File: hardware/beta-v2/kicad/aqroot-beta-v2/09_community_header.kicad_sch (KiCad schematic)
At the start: 36 parts, among them J5 COMMUNITY_HEADER_2x13, U15 TPS22918, U16 TCA9517ADGK

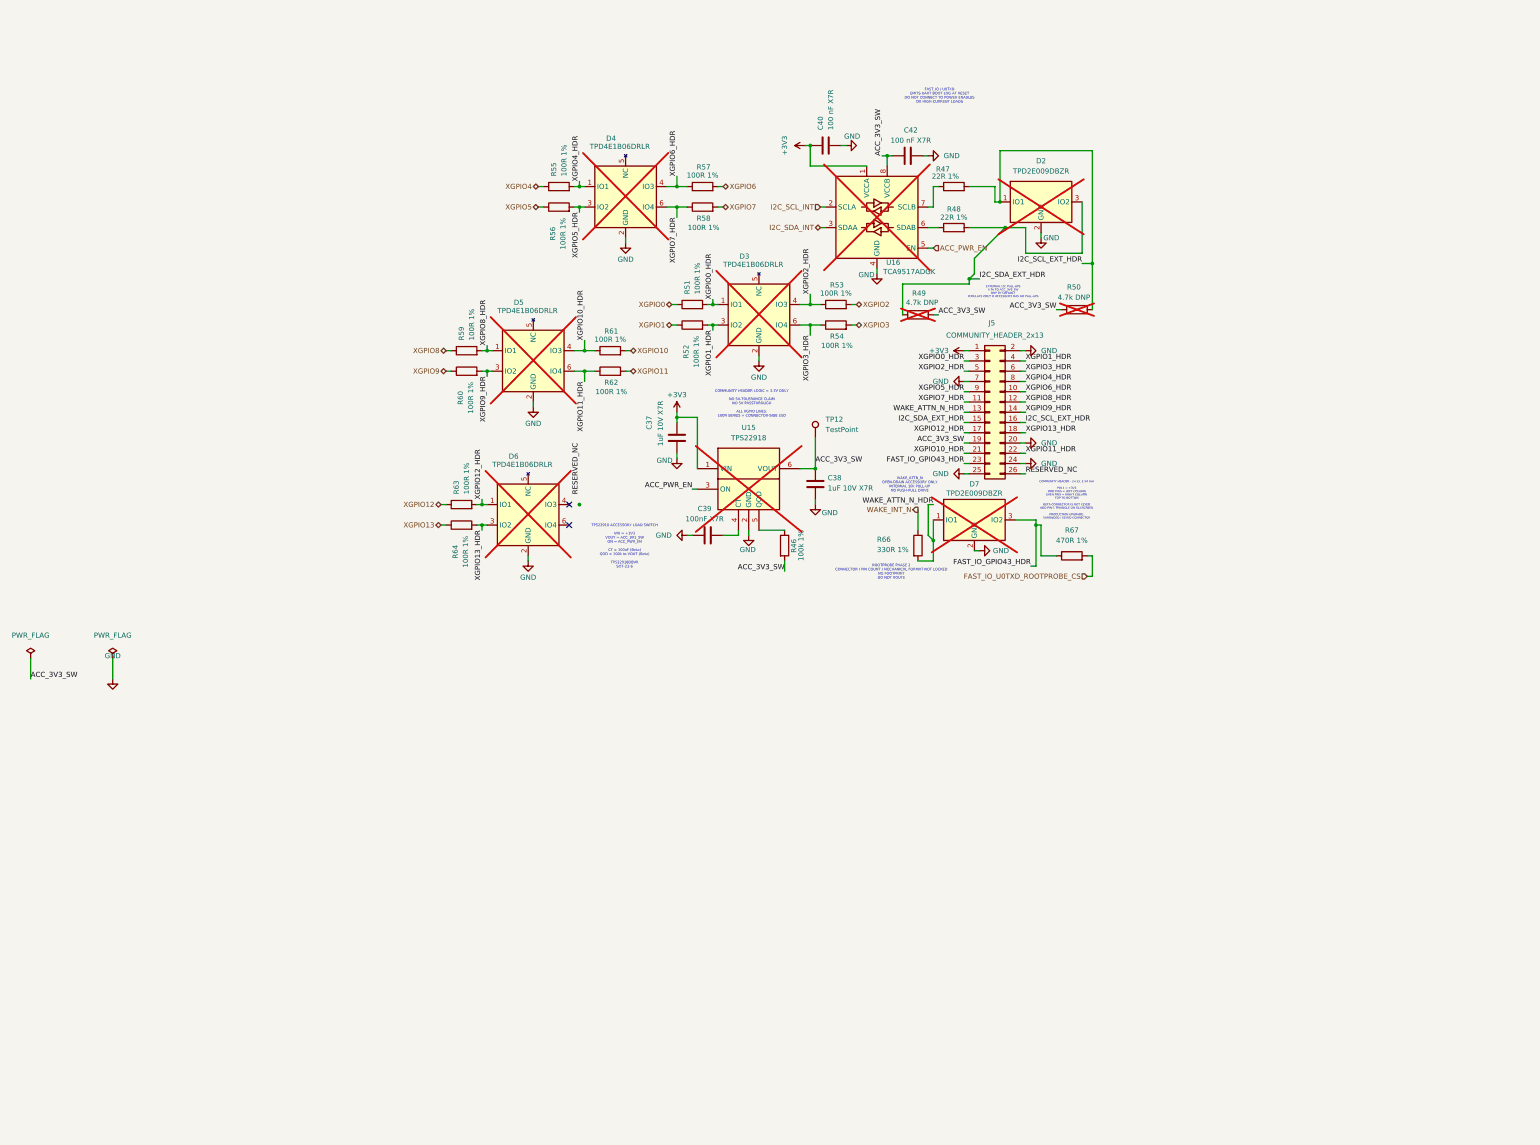
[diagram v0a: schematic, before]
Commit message: hardware: migrate Full Beta v2 community expansion
Sheet 09 migrated (FBV2-S1-009). All nine schematic sheets now carry the Full
Beta v2 architecture and fork_equivalence.py's "still Beta-DM" list is empty.

Three CTO rulings implemented. O-6 ratified: U23, the third PCAL9535APW,118 at
0x22, and the front RGB are locked architecture; B-37 retired with 11 spare
expander pins. O-4 approved: U16 TCA9517A -> TI TCA4307DGKR (LCSC C880333),
FITTED where the old part was DNP. P-18 closed with no I2C mux.

Sheet 09 was rebuilt, not patched, and was hiding two serious defects: J5
contact 1 carried permanent raw +3V3 against D-057, and the community port had
no power at all - 01:ACC_3V3_SW and 09:ACC_3V3_SW were different nets, the
latter fed by a second, DNP TPS22918. Also removed: the 26-pin 2x13 male
header, XGPIO10-13, FAST_IO_GPIO43_HDR, RESERVED_NC. Sixth consecutive sheet
with a load-bearing inherited DNP.

Connector footprint built from the Samtec RECOMMENDED PCB LAYOUT REV B FIG 3:
2.54 mm in row, 7.87 +/-0.05 mm row-to-row, 0.71 mm PTH, 27.94 mm pin field.
All 24 contacts verified pin by pin against D-084.

External I2C pull-ups re-derived: the inherited 4.7k gives 796 ns against a
300 ns fast-mode budget at 200 pF and could never have worked; now 1.5k =
254 ns. Both current limits re-derived rather than copied - 3.3 V stays 1.5k
but the accessory-short case moved 86% -> 89% of the TPS63020's 2 A.

5 V enables split per the CTO refinement: ACC_5V_BOOST_EN on U3 P13 and
ACC_5V_SW_EN on U23 P04, each with its own 100k pull-down. B-08 closed in
copper with Q10, source facing the connector. All six TVS arrays were DNP and
are now fitted; one TPD4E1B06DRLR MPN covers all sixteen exposed contacts.

#FLG0105, deleted by the rebuild, turned out to be the only power-output driver
on the entire GND net and was re-created with a note explaining its role.

ERC 42/1/41 -> 27/0/27 - zero errors for the first time. 321 components, 0
duplicate references, 0 without a footprint, 224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
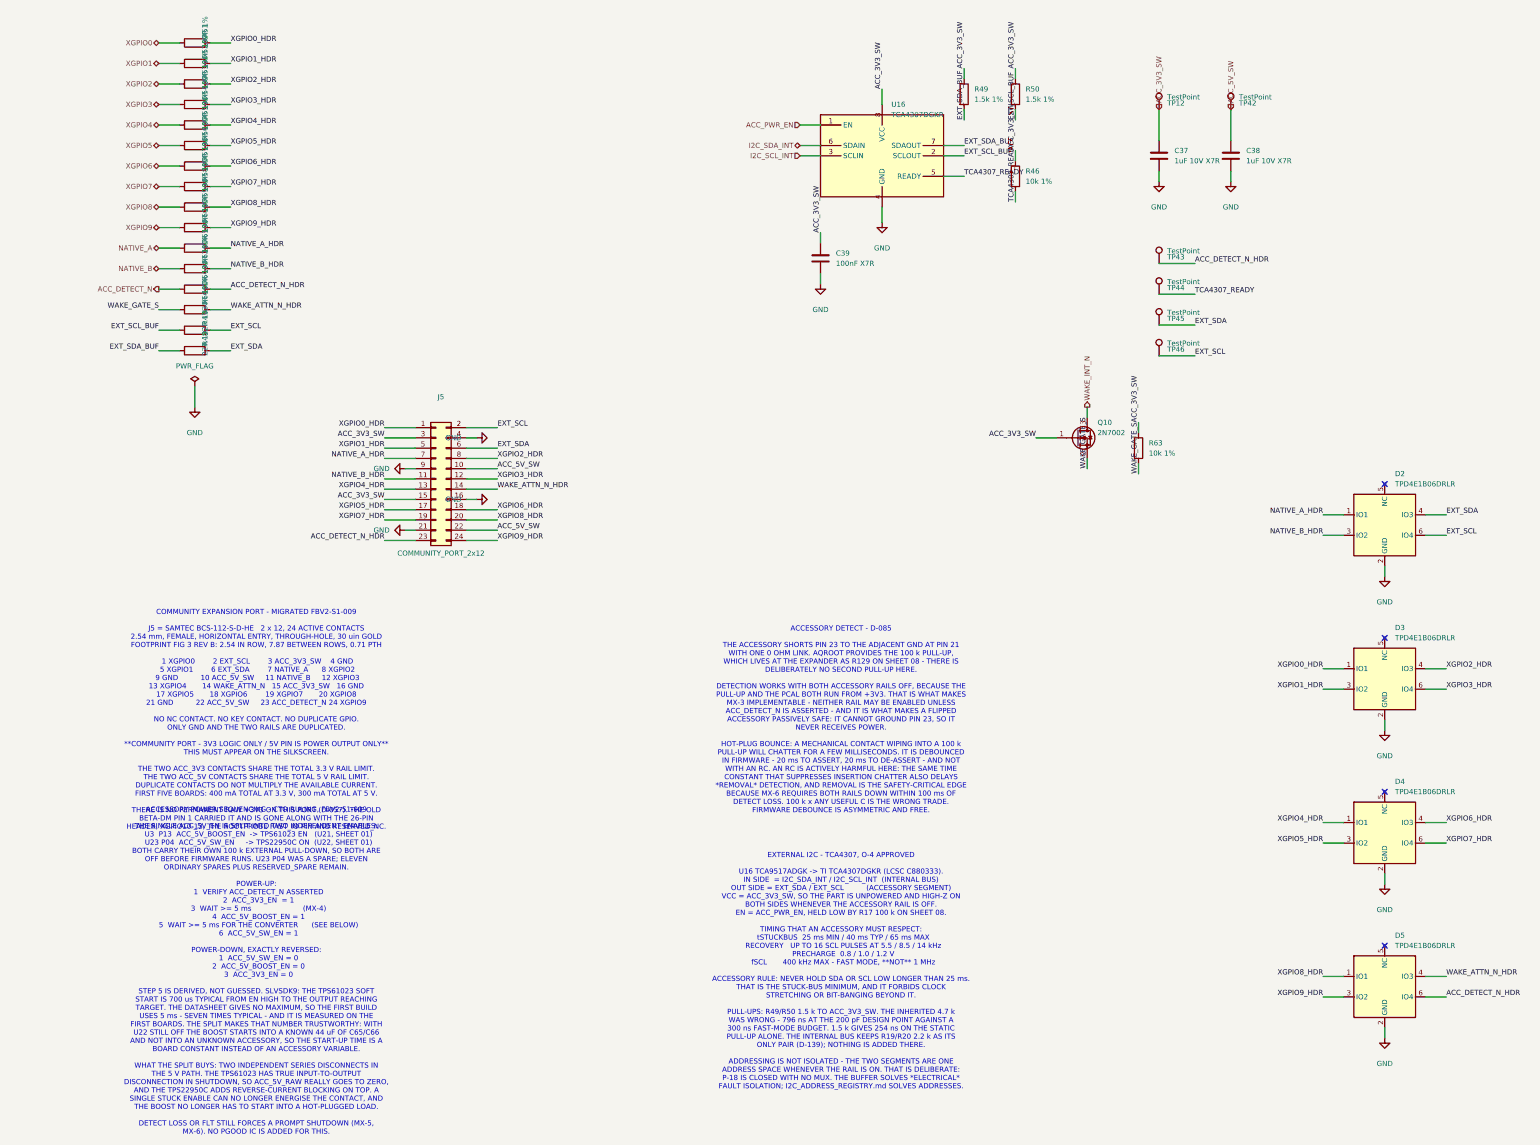
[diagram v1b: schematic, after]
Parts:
- removed C40, C42: 100 nF X7R, Capacitor_SMD:C_0603_1608Metric, symbol Device:C
- removed D2, D7: TPD2E009DBZR, Package_TO_SOT_SMD:SOT-23, symbol AQROOT_Beta:TPD2E009DBZR
- removed D6: TPD4E1B06DRLR, Package_TO_SOT_SMD:SOT-563, symbol AQROOT_Beta:TPD4E1B06DRLR
- removed J5: COMMUNITY_HEADER_2x13, AQROOT_Beta:Samtec_TSW-113-08-G-D-RA, symbol Connector_Generic:Conn_02x13_Odd_Even
- removed R67: 470R 1%, Resistor_SMD:R_0603_1608Metric, symbol Device:R
- removed U15: TPS22918, Package_TO_SOT_SMD:SOT-23-6, symbol AQROOT_Beta:TPS22918
- removed U16: TCA9517ADGK, Package_SO:VSSOP-8_3x3mm_P0.65mm, symbol Logic_LevelTranslator:TCA9517ADGK
- added D2: TPD4E1B06DRLR, Package_TO_SOT_SMD:SOT-563, symbol AQROOT_Beta:TPD4E1B06DRLR
- added J5: COMMUNITY_PORT_2x12, AQROOT_Beta:Samtec_BCS-112-S-D-HE, symbol Connector_Generic:Conn_02x12_Odd_Even
- added Q10: 2N7002, Package_TO_SOT_SMD:SOT-23, symbol Transistor_FET:Q_NMOS_GSD
- added TP42, TP43, TP44, TP45, TP46: TestPoint, TestPoint:TestPoint_Pad_D1.0mm, symbol Connector:TestPoint
- added U16: TCA4307DGKR, Package_SO:VSSOP-8_3x3mm_P0.65mm, symbol AQROOT_Beta:TCA4307DGKR
- C37: Note (none) -> Accessory 3.3 V rail decoupling AT THE CONNECTOR, FBV2-S1-0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
- C38: Note (none) -> Accessory 5 V rail decoupling AT THE CONNECTOR, FBV2-S1-009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
- C39: Note (none) -> TCA4307 local decoupling, FBV2-S1-009. 100 nF X7R 0603 agai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
- D3, D4, D5: Note Four independent bidirectional ESD channels. Place on the c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 -> Low-capacitance ESD array on the exposed community contacts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; Package SOT-563, TI DRL -> (none); now fitted
- R46: value 100k 1% -> 10k 1%; Note (none) -> TCA4307 READY pull-up, FBV2-S1-009. READY is an OPEN-DRAIN 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; Power (none) -> 0.1W; Tolerance (none) -> 1%
- R47, R48: Note (none) -> External I2C series element, D-090, RE-DERIVED FOR THE TCA4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; Power (none) -> 0.1W; Tolerance (none) -> 1%
- R49: value 4.7k DNP -> 1.5k 1%; Note (none) -> EXTERNAL I2C SDA pull-up, RE-DERIVED FBV2-S1-009. THE INHER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; Power (none) -> 0.1W; Tolerance (none) -> 1%; now fitted
- R50: value 4.7k DNP -> 1.5k 1%; Note (none) -> EXTERNAL I2C SCL pull-up, RE-DERIVED FBV2-S1-009. THE INHER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; Power (none) -> 0.1W; Tolerance (none) -> 1%; now fitted
- R51, R52, R53, R54, R55, R56, R57, R58, R59, R60: Note (none) -> Community XGPIO series protection, D-090. 100 Ohm between t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; Power (none) -> 0.1W; Tolerance (none) -> 1%
- R61, R62: Note (none) -> Native community pin series protection, D-090. 100 Ohm betw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; Power (none) -> 0.1W; Tolerance (none) -> 1%
- R63: value 100R 1% -> 10k 1%; Note (none) -> WAKE contact pull-up, FBV2-S1-009. 10 kOhm from the accesso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; Power (none) -> 0.1W; Tolerance (none) -> 1%
- R64: Note (none) -> ACC_DETECT_N series protection, ADDED FBV2-S1-009. D-090 di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; Power (none) -> 0.1W; Tolerance (none) -> 1%
- R66: Note (none) -> WAKE series protection, D-090. 330 Ohm rather than 100 Ohm 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; Power (none) -> 0.1W; Tolerance (none) -> 1%
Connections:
- net +3V3 is gone; now on net ACC_3V3_SW: C37.1
- net XGPIO12 is gone; now on net ACC_3V3_SW: R63.1
- net XGPIO13_HDR is gone; now on net ACC_DETECT_N_HDR: R64.2
- net ACC_3V3_SW: now also C39.1, R46.1, R49.1, R50.1, J5.15 (Pin_15), J5.3 (Pin_3), Q10.1 (G), U16.8 (VCC); no longer C38.1, R46.2, R49.2, R50.2
- net ACC_PWR_EN: now also U16.1 (EN)
- net GND: now also C39.2, D2.2 (GND), J5.16 (Pin_16), J5.21 (Pin_21), J5.4 (Pin_4), J5.9 (Pin_9), U16.4 (GND); no longer C39.1
- net I2C_SCL_INT: now also U16.3 (SCLIN)
- net I2C_SDA_INT: now also U16.6 (SDAIN)
- net WAKE_ATTN_N_HDR: now also D5.4 (IO3), J5.14 (Pin_14)
- net WAKE_INT_N: now also Q10.3 (D); no longer R66.1
- net XGPIO0_HDR: now also J5.1 (Pin_1)
- net XGPIO1_HDR: now also J5.5 (Pin_5)
- net XGPIO2: now also R53.1; no longer R53.2
- net XGPIO2_HDR: now also R53.2, J5.8 (Pin_8); no longer R53.1
- net XGPIO3: now also R54.1; no longer R54.2
- net XGPIO3_HDR: now also R54.2, J5.12 (Pin_12); no longer R54.1
- net XGPIO4_HDR: now also J5.13 (Pin_13)
- net XGPIO5_HDR: now also J5.17 (Pin_17)
- net XGPIO6: now also R57.1; no longer R57.2
- net XGPIO6_HDR: now also R57.2, J5.18 (Pin_18); no longer R57.1
- net XGPIO7: now also R58.1; no longer R58.2
- net XGPIO7_HDR: now also R58.2, J5.19 (Pin_19); no longer R58.1
- net XGPIO8_HDR: now also J5.20 (Pin_20)
- net XGPIO9_HDR: now also J5.24 (Pin_24)
- net EXT_SCL_BUF: now reaches R47.1
- net EXT_SCL_BUF: now also R50.2, U16.2 (SCLOUT)
- net EXT_SDA_BUF: now reaches R48.1
- net EXT_SDA_BUF: now also R49.2, U16.7 (SDAOUT)
- net I2C_SCL_EXT_HDR renamed EXT_SCL
- net EXT_SCL: now also D2.6 (IO4), J5.2 (Pin_2), TP46.1; no longer R50.1
- net I2C_SDA_EXT_HDR renamed EXT_SDA
- net EXT_SDA: now also D2.4 (IO3), J5.6 (Pin_6), TP45.1; no longer R49.1
- net XGPIO10 renamed NATIVE_A_HDR
- net NATIVE_A_HDR: now also D2.1 (IO1), J5.7 (Pin_7)
- net XGPIO10_HDR renamed NATIVE_A
- net NATIVE_A: no longer D5.4 (IO3)
- net XGPIO11 renamed NATIVE_B_HDR
- net NATIVE_B_HDR: now also D2.3 (IO2), J5.11 (Pin_11)
- net XGPIO11_HDR renamed ACC_DETECT_N_HDR
- net ACC_DETECT_N_HDR: now also J5.23 (Pin_23), TP43.1; no longer R62.1
- net XGPIO12_HDR renamed WAKE_GATE_S
- net WAKE_GATE_S: now also R66.1, Q10.2 (S)
- net XGPIO13 renamed ACC_DETECT_N
- new net ACC_5V_SW: C38.1, J5.10 (Pin_10), J5.22 (Pin_22), TP42.1
- new net NATIVE_B: R62.1
- new net TCA4307_READY: R46.2, TP44.1, U16.5 (READY)
- no-connect marks 2 -> 4
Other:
- note added: "ACCESSORY DETECT - D-085 THE ACCESSORY SHORTS PIN 23 TO THE ADJACENT GND AT PIN 21 WITH ONE 0 OHM LINK. AQROOT PROVIDES THE 100 k PULL-UP, WHICH LIVES AT THE EXPANDER AS R129 ON SHEET 08 - THERE IS DELIBERATELY NO SECOND PULL-UP HERE. DETECTION WORKS WITH BOTH ACCESSORY RAILS OFF, BECAUSE THE PULL-UP AND THE PCAL BOTH RUN FROM +3V3. THAT IS WHAT MAKES MX-3 IMPLEMENTABLE - NEITHER RAIL MAY BE ENAB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"
- note added: "ACCESSORY POWER SEQUENCING - CTO RULING, FBV2-S1-009 THE SINGLE ACC_5V_EN IS SPLIT INTO TWO INDEPENDENT ENABLES: U3 P13 ACC_5V_BOOST_EN -> TPS61023 EN (U21, SHEET 01) U23 P04 ACC_5V_SW_EN -> TPS22950C ON (U22, SHEET 01) BOTH CARRY THEIR OWN 100 k EXTERNAL PULL-DOWN, SO BOTH ARE OFF BEFORE FIRMWARE RUNS. U23 P04 WAS A SPARE; ELEVEN ORDINARY SPARES PLUS RESERVED_SPARE REMAIN. POWER-UP: 1 VERIFY ACC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"
- note added: "COMMUNITY EXPANSION PORT - MIGRATED FBV2-S1-009 J5 = SAMTEC BCS-112-S-D-HE 2 x 12, 24 ACTIVE CONTACTS 2.54 mm, FEMALE, HORIZONTAL ENTRY, THROUGH-HOLE, 30 uin GOLD FOOTPRINT FIG 3 REV B: 2.54 IN ROW, 7.87 BETWEEN ROWS, 0.71 PTH 1 XGPIO0 2 EXT_SCL 3 ACC_3V3_SW 4 GND 5 XGPIO1 6 EXT_SDA 7 NATIVE_A 8 XGPIO2 9 GND 10 ACC_5V_SW 11 NATIVE_B 12 XGPIO3 13 XGPIO4 14 WAKE_ATTN_N 15 ACC_3V3_SW 16 GND 17 XGPIO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"
- note added: "EXTERNAL I2C - TCA4307, O-4 APPROVED U16 TCA9517ADGK -> TI TCA4307DGKR (LCSC C880333). IN SIDE = I2C_SDA_INT / I2C_SCL_INT (INTERNAL BUS) OUT SIDE = EXT_SDA / EXT_SCL (ACCESSORY SEGMENT) VCC = ACC_3V3_SW, SO THE PART IS UNPOWERED AND HIGH-Z ON BOTH SIDES WHENEVER THE ACCESSORY RAIL IS OFF. EN = ACC_PWR_EN, HELD LOW BY R17 100 k ON SHEET 08. TIMING THAT AN ACCESSORY MUST RESPECT: tSTUCKBUS 25 ms M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"
- note removed: "COMMUNITY HEADER - 2×13, 2.54 mm PIN 1 = +3V3 ODD PINS = LEFT COLUMN EVEN PINS = RIGHT COLUMN TOP TO BOTTOM BETA CONNECTOR IS NOT KEYED ADD PIN-1 TRIANGLE ON SILKSCREEN PRODUCTION UPGRADE: SHROUDED / KEYED CONNECTOR"
- note removed: "COMMUNITY HEADER LOGIC = 3.3V ONLY NO 5V-TOLERANCE CLAIM NO 5V PASSTHROUGH ALL XGPIO LINES: 100R SERIES + CONNECTOR-SIDE ESD"
- note removed: "EXTERNAL I2C PULL-UPS 4.7k TO ACC_3V3_SW DNP BY DEFAULT POPULATE ONLY IF ACCESSORY HAS NO PULL-UPS"
- note removed: "FAST_IO / U0TXD EMITS UART BOOT LOG AT RESET DO NOT CONNECT TO POWER ENABLES OR HIGH-CURRENT LOADS"
- note removed: "ROOTPROBE PHASE 2 CONNECTOR / PIN COUNT / MECHANICAL FORMAT NOT LOCKED NO FOOTPRINT DO NOT ROUTE"
- note removed: "TPS22918 ACCESSORY LOAD SWITCH VIN = +3V3 VOUT = ACC_3V3_SW ON = ACC_PWR_EN CT = 100nF (Beta) QOD = 100k to VOUT (Beta) TPS22918DBVR SOT-23-6"
- note removed: "WAKE_ATTN_N OPEN-DRAIN ACCESSORY ONLY INTERNAL 10k PULL-UP NO PUSH-PULL DRIVE"

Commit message: hardware: close Full Beta v2 S2 release blockers
Closes B-03, B-63, B-70 and B-71's schematic-side work. Property-only
changes to the nine sheets plus the microphone footprint; ERC unchanged
at 27 / 0 errors / 27 with an identical violation histogram, and the PCB
is untouched and still bit-identical to Beta-DM.

B-03 - all eight remaining Tier-2 footprints compared dimension by
dimension against retrieved manufacturer drawings. Y1 moves from
candidate to lock (Yajingxin TXM27.12M0004322DBBDO00T, C362365, 3421 in
stock) with a land that matches the vendor's Suggested Layout exactly.
The MAX98357A looked like a genuine defect - outline 21-0136 gives
T1633-5 an EP of 1.50/1.60/1.70 while the land is 1.23 - and is not:
land pattern 90-0032 Rev E is issued for T1633-5, -5C and -7C together
and specifies one land for all three, so no project-local footprint was
created.

B-63 - the microphone acoustic port is now drawn rather than described.
1.05 mm NPTH taken from the drawing's own pad-4 ring inner diameter,
paste pulled back 0.10 mm as a declared stencil choice, keepout marked,
bottom-port orientation recorded.

B-70 - L5/L6 lock to Murata LQW18AN39NG80D. The DCR is a first-order
term here: 0.20 ohm max against R_q = 1.1 ohm drops network Q from 25.3
to about 21.4, so the antenna must be tuned with this exact part fitted
and the first lever is R_q, not 39 nH.

B-71 - 65 LCSC fields written in, three MPN strings corrected. J6 and J7
carried bare order codes that resolve to zero-stock listings while the
plating-suffixed strings are abundantly stocked. Six substitution traps
recorded in the symbols themselves, including BAT54W offered for
BAT54WS - a single diode for a series pair - and a clone for the battery
reverse-polarity pass FETs.

Eight DNP parts still carried no recorded reason and now do. The design
has zero unexplained DNP.

Co-Authored-By: Claude Opus 5 <noreply@anthropic.com>
Claude-Session: https://claude.ai/code/session_0133CdFHfKcCH8oPWqJZWe7o
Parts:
- D2, D3, D4, D5: LCSC (none) -> C1972953
- J5: LCSC (none) -> C5575816; Note2 (none) -> SOURCING 2026-08-23 (FBV2-S2-002) (B-71). Samtec BCS-112-S-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
- Q10: LCSC (none) -> C8545
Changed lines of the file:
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@@
 			)
 		)
+		(property "Note2" "SOURCING 2026-08-23 (FBV2-S2-002) (B-71). Samtec BCS-112-S-D-HE is LCSC C5575816 with STOCK 0 at $15.54. It is a 24-contact through-hole strip and was already MANUAL/SECONDARY ASSEMBLY by CTO ruling at FBV2-S1-009; buy direct from Samtec or a broadline distributor. The connector architecture is NOT compromised for SMT assembly. LCSC/JLC library state verified live on 2026-08-23 through the JLCPCB parts API (D-096). Stock is a snapshot, not a guarantee."
+			(at 120.65 140.97 0)
+			(hide yes)
+			(show_name no)
+			(do_not_autoplace no)
+			(effects
+				(font
+					(size 1.27 1.27)
+				)
+			)
+		)
+		(property "LCSC" "C5575816"
+			(at 120.65 140.97 0)
+			(hide yes)
+			(show_name no)
+			(do_not_autoplace no)
+			(effects
+				(font
+					(size 1.27 1.27)
+				)
+			)
+		)
 		(property "Manufacturer" "Samtec"
 			(at 0 0 0)
@@
 			)
 		)
+		(property "LCSC" "C8545"
+			(at 279.4 130.81 0)
+			(hide yes)
+			(show_name no)
+			(do_not_autoplace no)
+			(effects
+				(font
+					(size 1.27 1.27)
+				)
+			)
+		)
 		(property "Manufacturer" "onsemi"
 			(at 0 0 0)
@@
 			)
 		)
+		(property "LCSC" "C1972953"
+			(at 355.6 152.4 0)
+			(hide yes)
+			(show_name no)
+			(do_not_autoplace no)
+			(effects
+				(font
+					(size 1.27 1.27)
+				)
+			)
+		)
 		(property "Manufacturer" "Texas Instruments"
 			(at 0 0 0)
@@
 			)
 		)
+		(property "LCSC" "C1972953"
+			(at 355.6 190.5 0)
+			(hide yes)
+			(show_name no)
+			(do_not_autoplace no)
+			(effects
+				(font
+					(size 1.27 1.27)
+				)
+			)
+		)
 		(property "Manufacturer" "Texas Instruments"
 			(at 0 0 0)
@@
 			)
 		)
+		(property "LCSC" "C1972953"
+			(at 355.6 228.6 0)
+			(hide yes)
+			(show_name no)
+			(do_not_autoplace no)
+			(effects
+				(font
+					(size 1.27 1.27)
+				)
+			)
+		)
 		(property "Manufacturer" "Texas Instruments"
 			(at 0 0 0)
@@
 			(at 355.6 266.7 0)
 			(hide yes)
+			(show_name no)
+			(do_not_autoplace no)
+			(effects
+				(font
+					(size 1.27 1.27)
+				)
+			)
+		)
+		(property "LCSC" "C1972953"
+			(at 355.6 266.7 0)
+			(hide yes)
